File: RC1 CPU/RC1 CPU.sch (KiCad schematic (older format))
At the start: 37 parts, among them K1 SW_SPST, K2 SW_SPST, U1 WD65C02, U15 74LS00, U16 74LS04, U2 6532_A, U3 6532_B, U4 74LS145, U7 74LS145, X1 ACO-xxxMHz

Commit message: RAM
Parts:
- added JP6: K1_RAM, symbol Jumper_NO_Small
- added JP7: K2_RAM, symbol Jumper_NO_Small
- added JP8: K3_RAM, symbol Jumper_NO_Small
- added JP9: K4_RAM, symbol Jumper_NO_Small
- added JP?: RAM_A13, symbol Jumper_NC_Dual
- added JP?: RAM_A14, symbol Jumper_NC_Dual
- added U?: HM62256BLP-7, DIP28, symbol HM62256BLP-7
- added U?: 74LS00, symbol 74LS00
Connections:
- net labels added: RAM_CS, RAM_WE
- wire segments 212 -> 260

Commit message: Single Step Circuit
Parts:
- removed K1, K2: SW_SPST, symbol SW_SPST
- added K1, K2: SW_Push, symbol SW_Push
- added K25: SW_SPST, symbol SW_SPST
- added R7: 10, symbol R
- added U26: 74LS00, symbol 74LS00
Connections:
- net labels added: SST
- wire segments 260 -> 268

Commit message: ...
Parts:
- added JP10: B_PB7_IRQ, symbol Jumper_NO_Small
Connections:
- net labels added: A_PA0, A_PA1, A_PA2, A_PA3, A_PA4, A_PA5, A_PA6, A_PA7, A_PB0, A_PB1, A_PB2, A_PB3, A_PB4, A_PB5, A_PB6, A_PB7, B_PA0, B_PA1, B_PA2, B_PA3, B_PA4, B_PA5, B_PA6, B_PA7, B_PB0, B_PB1, B_PB2, B_PB3, B_PB4, B_PB5, B_PB6, B_PB7
- wire segments 268 -> 310
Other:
- moved on the sheet: JP5

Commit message: CPU schematic drafted
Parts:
- removed C3: 220nF, symbol C
- removed JP10: B_PB7_IRQ, symbol Jumper_NO_Small
- removed JP3: K2_ROM, symbol Jumper_NO_Small
- removed JP4: IRQ_EN_A, symbol Jumper_NO_Small
- removed JP5: IRQ_EN_B, symbol Jumper_NO_Small
- removed JP6: K1_RAM, symbol Jumper_NO_Small
- removed JP7: K2_RAM, symbol Jumper_NO_Small
- removed JP8: K3_RAM, symbol Jumper_NO_Small
- removed JP9: K4_RAM, symbol Jumper_NO_Small
- removed JP?: VP_GND, symbol Jumper_NO_Small
- removed JP?: ROM_A14, symbol Jumper_NC_Dual
- removed JP?: ROM_A13, symbol Jumper_NC_Dual
- removed JP?: RAM_A13, symbol Jumper_NC_Dual
- removed JP?: RAM_A14, symbol Jumper_NC_Dual
- removed K1, K2: SW_Push, symbol SW_Push
- removed K25: SW_SPST, symbol SW_SPST
- removed R13: 1k, symbol R
- removed R25, R?: 47k, symbol R
- removed R35, R36, R38, R39: 560, symbol R
- removed R?: 3.3k, symbol R
- removed R?: 3k3, symbol R
- removed U1: WD65C02, symbol WD65C02
- removed U15, U26, U?: 74LS00, symbol 74LS00
- removed U16: 74LS04, symbol 74LS04
- removed U2: 6532_A, symbol R6532
- removed U4: 74LS145, symbol 74LS145
- removed U? (x2): NE555, symbol NE555
- removed U?: 28C256, symbol 28C256
- removed U?: HM62256BLP-7, DIP28, symbol HM62256BLP-7
- added C1: 220nF, symbol C
- added J1: Expansion, Pin_Headers:Pin_Header_Angled_1x39_Pitch2.54mm, symbol RC1_Backplane
- added J2: RC1_UI_Port, Pin_Headers:Pin_Header_Straight_2x20_Pitch2.54mm, symbol RC1_UI_Port
- added J3: BARREL_JACK, Connectors:BARREL_JACK, symbol BARREL_JACK
- added M1, M2, M3, M4: Mounting, mounting:1pin, symbol Mounting
- added R10, R5, R8, R9: 1k, symbol R
- added R11: 47k, symbol R
- added R6: 3k3, symbol R
- added U1: HM62256BLP-7, DIP28, symbol HM62256BLP-7
- added U2: 28C256, symbol 28C256
- added U4: WD65C02, symbol WD65C02
- added U5, U9: 74LS00, symbol 74LS00
- added U6: LM556, symbol LM556
- added U8: 74LS138, symbol 74LS138
- JP1: value K4_ROM -> VP_GND
- JP2: value K3_ROM -> DEN
- R12: value 1k -> 47k
- R3: value 3k3 -> 3.3k
- R4: value 3k3 -> 1k
- R7: value 10 -> 3k3
- U3: value 6532_B -> 6532
- X1: value ACO-xxxMHz -> 1MHz
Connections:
- net labels added: BE, DEN, IO2, IO3, PA0, PA1, PA2, PA3, PA4, PA5, PA6, PA7, PB0, PB1, PB2, PB3, PB4, PB5, PB6, PB7, PHI0, PHI2, RAM_SEL, RS, ST, ~A4
- net labels removed: A_PA0, A_PA1, A_PA2, A_PA3, A_PA4, A_PA5, A_PA6, A_PA7, A_PB0, A_PB1, A_PB2, A_PB3, A_PB4, A_PB5, A_PB6, A_PB7, B_PA0, B_PA1, B_PA2, B_PA3, B_PA4, B_PA5, B_PA6, B_PA7, B_PB0, B_PB1, B_PB2, B_PB3, B_PB4, B_PB5, B_PB6, B_PB7, CLK0, CLK1, CLK2, DECEN, K1, K2, K3, K4, R0, RAMRW, RAM_CS, RAM_WE, ROM_CE, SST, ~R/W
- wire segments 310 -> 303
- no-connect marks 21 -> 32

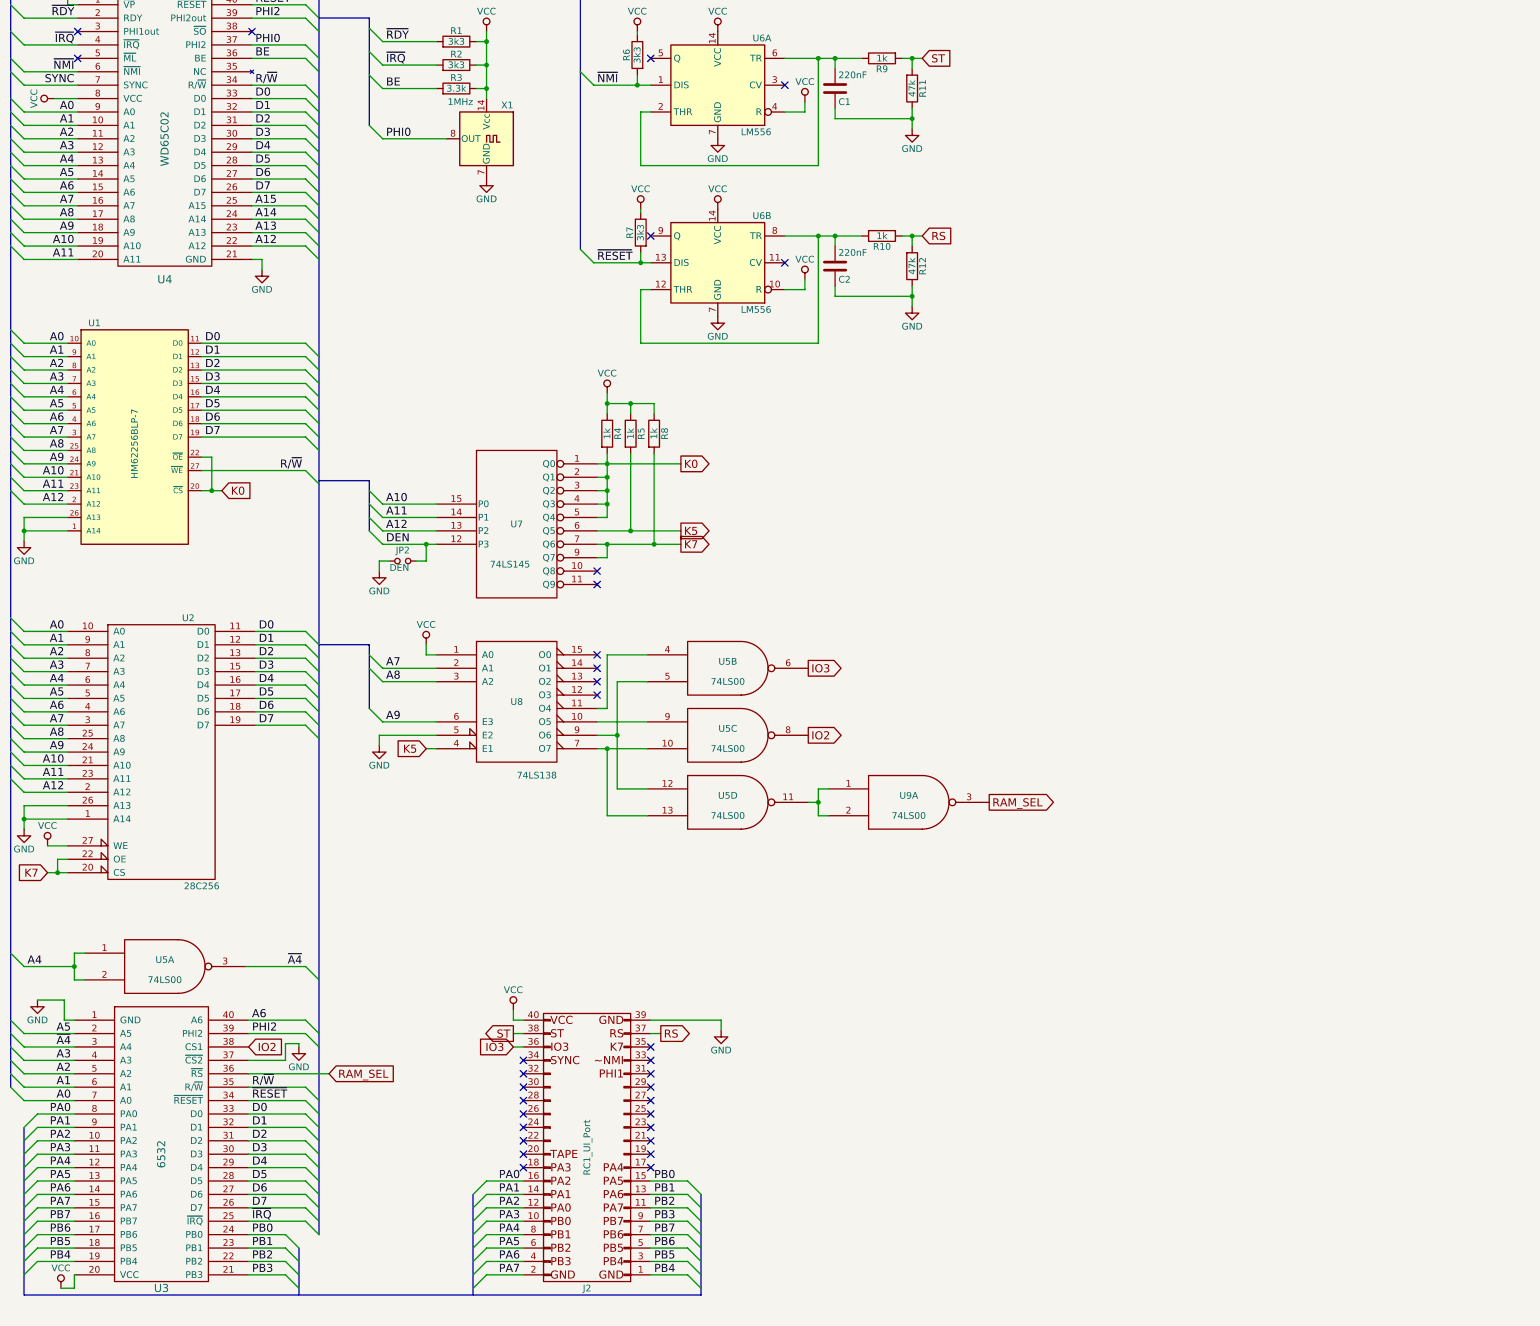
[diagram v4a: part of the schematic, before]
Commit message: Added bypass caps and leftover gates
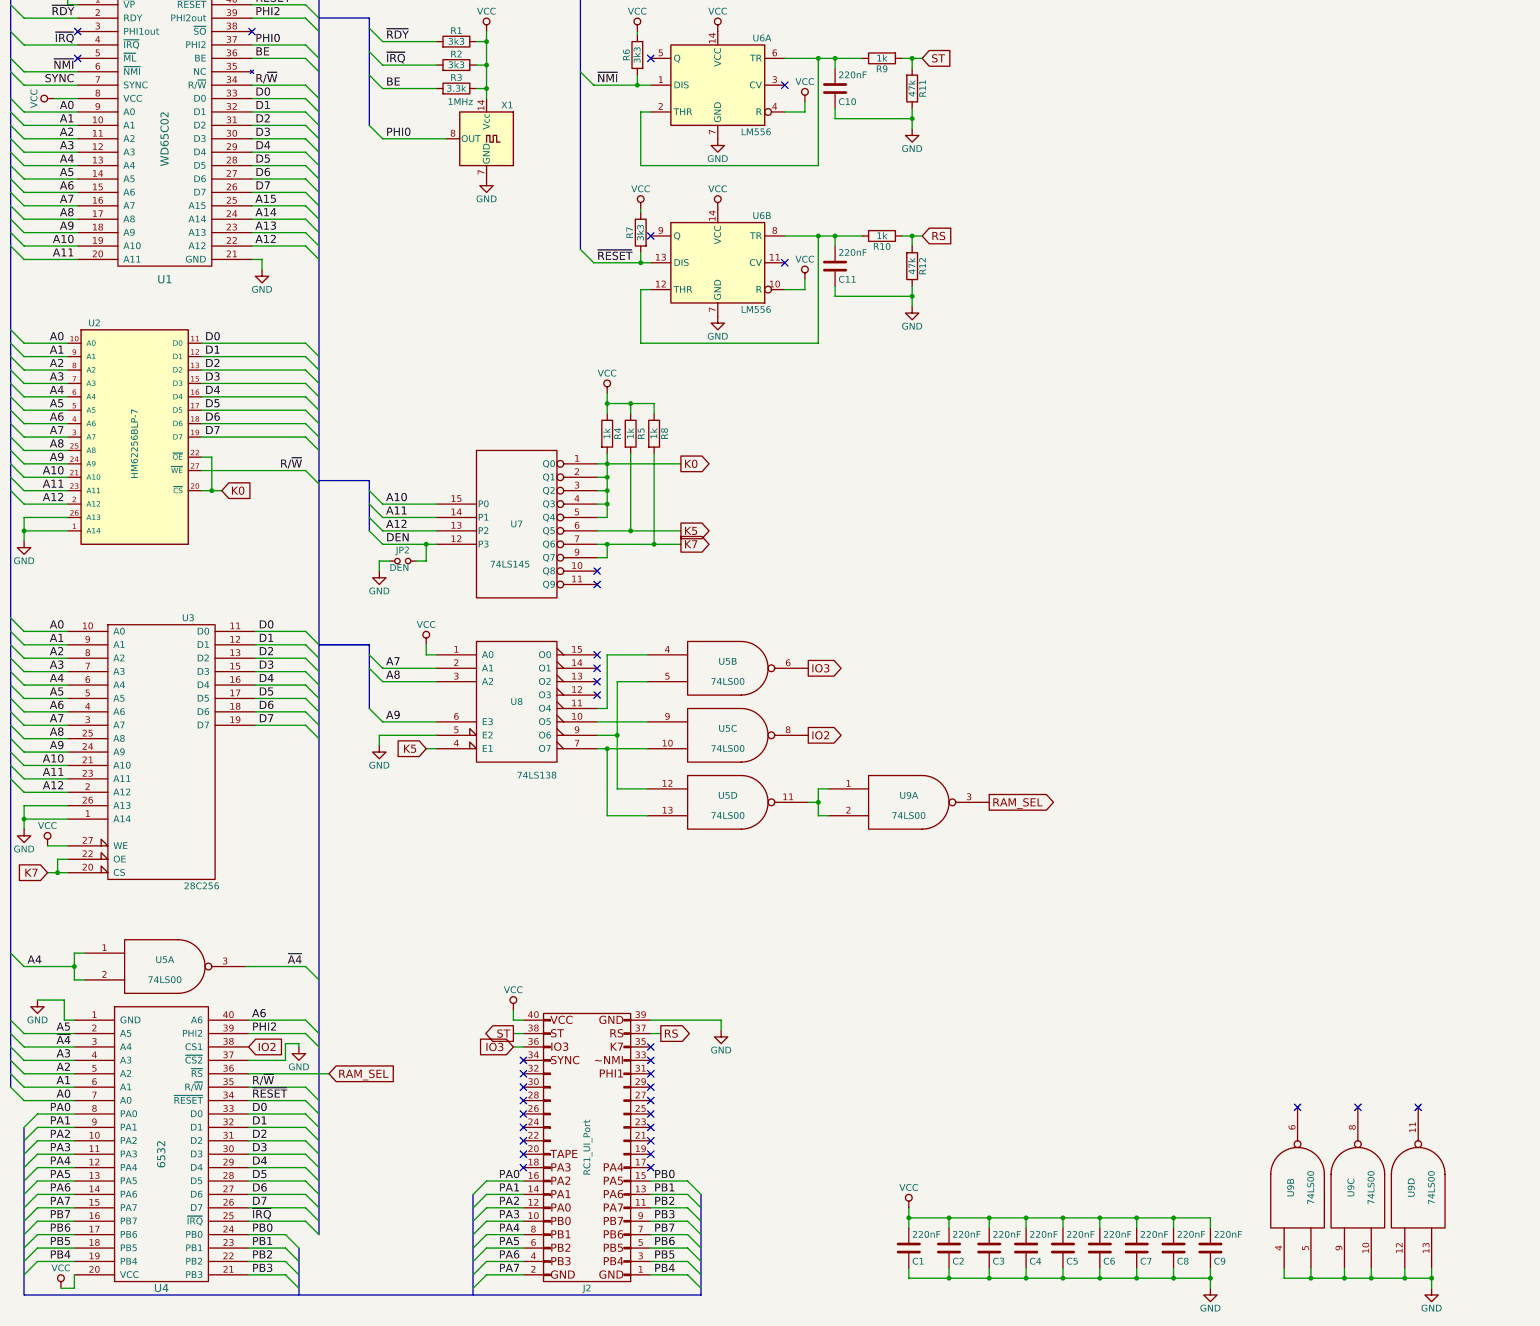
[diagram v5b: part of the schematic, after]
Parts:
- added C1, C2, C3, C4, C5, C6, C7, C8, C9: 220nF, symbol C
- added unit 2 of U9
- added unit 3 of U9
- added unit 4 of U9
- renumbered C1 to C10, C2 to C11, U4 to U1, U1 to U2, U2 to U3, U3 to U4
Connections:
- net GND: now also C1.1, C2.1, C3.1, C4.1, C5.1, C6.1, C7.1, C8.1, C9.1, U9.10, U9.12, U9.13, U9.4, U9.5, U9.7 (GND), U9.7 (GND), U9.7 (GND), U9.9
- net VCC: now also C1.2, C2.2, C3.2, C4.2, C5.2, C6.2, C7.2, C8.2, C9.2, U9.14 (VCC), U9.14 (VCC), U9.14 (VCC)
- no-connect marks 32 -> 35
